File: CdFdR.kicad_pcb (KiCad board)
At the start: 2 copper layers, 64.8 x 90.2 mm, 17 parts, among them J1 Moteur_1, J2 Moteur_2, J3 Moteur_3, J4 Moteur_4, U1 ESP32-S3-N16R8-DEVBOARD

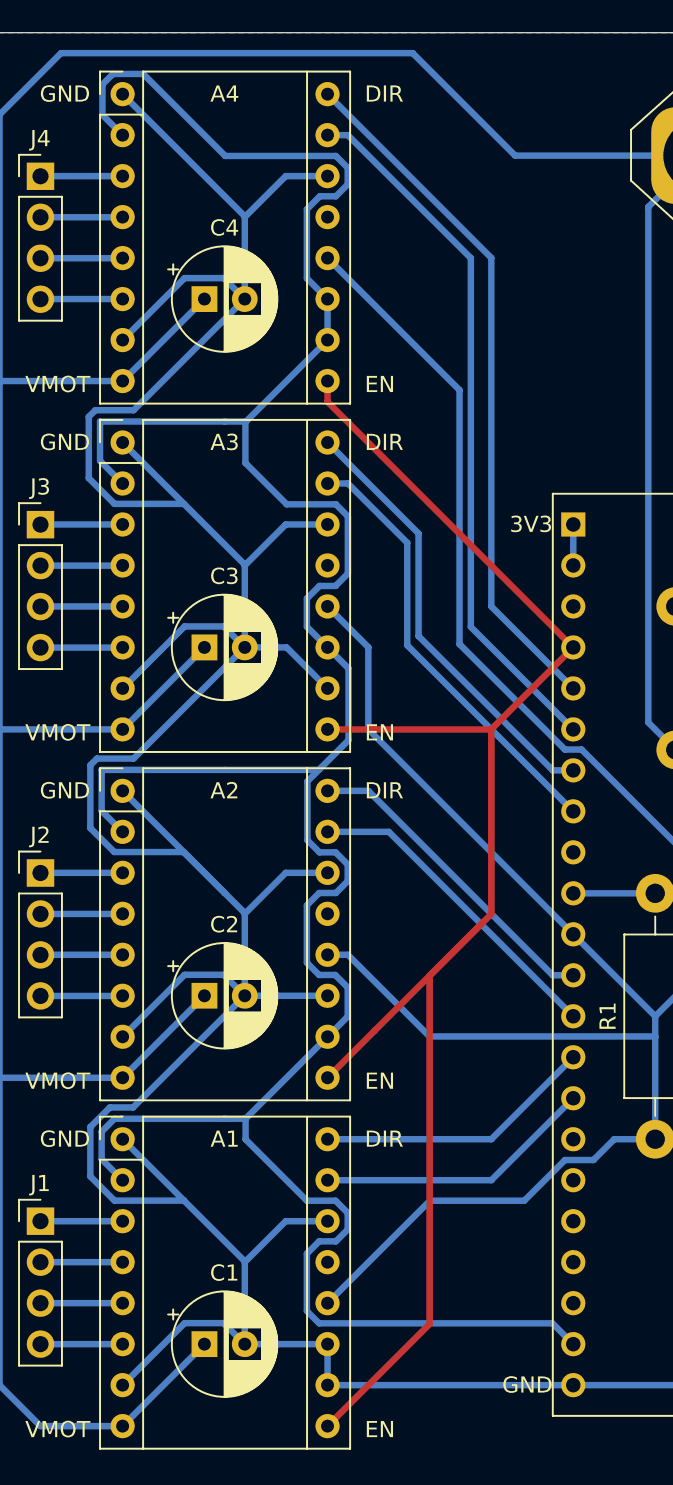
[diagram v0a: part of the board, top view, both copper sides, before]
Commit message: Changed drivers uart code due to error on hand soldered board
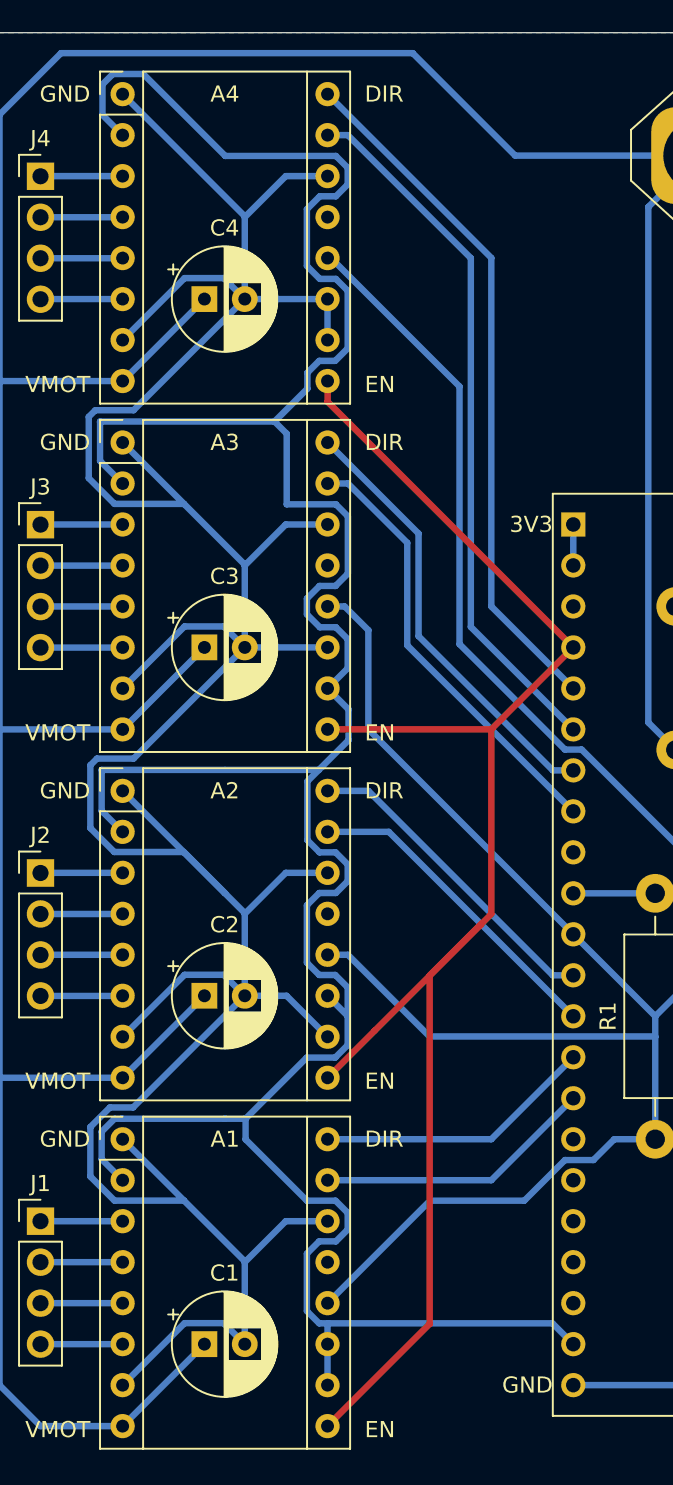
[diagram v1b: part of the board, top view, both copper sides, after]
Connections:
- A1 pad 10: GND -> +5V
- A1 pad 11: GND -> +5V
- A2 pad 10: +5V -> GND
- A2 pad 11: GND -> +5V
- A3 pad 10: GND -> +5V
- A3 pad 11: +5V -> GND
- A4 pad 10: +5V -> GND
- A4 pad 11: +5V -> GND
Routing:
- net GND: track 358.9 -> 343.6 mm
- net +5V: track 179.2 -> 190.0 mm
- net UART_Mot: track 145.8 -> 146.5 mm

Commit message: Correction des pins des moteurs pour être en accord avec carte soudé
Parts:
- A1: value Pololu_Breakout -> M4
- A2: value Pololu_Breakout -> M3
- A3: value Pololu_Breakout -> M2
- A4: value Pololu_Breakout -> M1
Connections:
- A1 pad 15: M1_STP -> M4_STP
- A1 pad 16: M1_DIR -> M4_DIR
- A2 pad 15: M2_STP -> M3_STP
- A2 pad 16: M2_DIR -> M3_DIR
- A3 pad 15: M3_STP -> M2_STP
- A3 pad 16: M3_DIR -> M2_DIR
- A4 pad 15: M4_STP -> M1_STP
- A4 pad 16: M4_DIR -> M1_DIR
- U1 pad 12: M2_DIR -> M3_DIR
- U1 pad 13: M2_STP -> M3_STP
- U1 pad 14: M1_DIR -> M4_DIR
- U1 pad 15: M1_STP -> M4_STP
- U1 pad 5: M4_DIR -> M1_DIR
- U1 pad 6: M4_STP -> M1_STP
- U1 pad 7: M3_DIR -> M2_DIR
- U1 pad 8: M3_STP -> M2_STP
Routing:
- net M4_STP: track 43.9 -> 17.3 mm
- net M1_STP: track 17.3 -> 43.9 mm
- net M4_DIR: track 43.1 -> 17.3 mm
- net M1_DIR: track 17.3 -> 43.1 mm
- net M3_DIR: track 27.4 -> 20.0 mm
- net M2_DIR: track 20.0 -> 27.4 mm
- net M3_STP: track 27.4 -> 20.0 mm
- net M2_STP: track 20.0 -> 27.4 mm
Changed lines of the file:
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@@
 			)
 		)
-		(property "Value" "Pololu_Breakout"
+		(property "Value" "M4"
 			(at 6.35 20.17 0)
 			(layer "F.Fab")
@@
 			(layers "*.Cu" "*.Mask")
 			(remove_unused_layers no)
-			(net 9 "M1_STP")
+			(net 28 "M4_STP")
 			(pinfunction "STEP")
 			(pintype "input")
@@
 			(layers "*.Cu" "*.Mask")
 			(remove_unused_layers no)
-			(net 11 "M1_DIR")
+			(net 33 "M4_DIR")
 			(pinfunction "DIR")
 			(pintype "input")
@@
 			)
 		)
-		(property "Value" "Pololu_Breakout"
+		(property "Value" "M2"
 			(at 6.35 20.17 0)
 			(layer "F.Fab")
@@
 			(layers "*.Cu" "*.Mask")
 			(remove_unused_layers no)
-			(net 22 "M3_STP")
+			(net 18 "M2_STP")
 			(pinfunction "STEP")
 			(pintype "input")
@@
 			(layers "*.Cu" "*.Mask")
 			(remove_unused_layers no)
-			(net 24 "M3_DIR")
+			(net 13 "M2_DIR")
 			(pinfunction "DIR")
 			(pintype "input")
@@
 			)
 		)
-		(property "Value" "Pololu_Breakout"
+		(property "Value" "M3"
 			(at 6.35 20.17 0)
 			(layer "F.Fab")
@@
 			(layers "*.Cu" "*.Mask")
 			(remove_unused_layers no)
-			(net 18 "M2_STP")
+			(net 22 "M3_STP")
 			(pinfunction "STEP")
 			(pintype "input")
@@
 			(layers "*.Cu" "*.Mask")
 			(remove_unused_layers no)
-			(net 13 "M2_DIR")
+			(net 24 "M3_DIR")
 			(pinfunction "DIR")
 			(pintype "input")
@@
 			)
 		)
-		(property "Value" "Pololu_Breakout"
+		(property "Value" "M1"
 			(at 6.35 20.17 0)
 			(layer "F.Fab")
@@
 			(layers "*.Cu" "*.Mask")
 			(remove_unused_layers no)
-			(net 28 "M4_STP")
+			(net 9 "M1_STP")
 			(pinfunction "STEP")
 			(pintype "input")
@@
 			(layers "*.Cu" "*.Mask")
 			(remove_unused_layers no)
-			(net 33 "M4_DIR")
+			(net 11 "M1_DIR")
 			(pinfunction "DIR")
 			(pintype "input")
@@
 			(keep_end_layers yes)
 			(zone_layer_connections)
-			(net 33 "M4_DIR")
+			(net 11 "M1_DIR")
 			(pinfunction "5")
 			(pintype "bidirectional")
@@
 			(keep_end_layers yes)
 			(zone_layer_connections)
-			(net 28 "M4_STP")
+			(net 9 "M1_STP")
 			(pinfunction "6")
 			(pintype "bidirectional")
@@
 			(keep_end_layers yes)
 			(zone_layer_connections)
-			(net 24 "M3_DIR")
+			(net 13 "M2_DIR")
 			(pinfunction "7")
 			(pintype "bidirectional")
@@
 			(keep_end_layers yes)
 			(zone_layer_connections)
-			(net 22 "M3_STP")
+			(net 18 "M2_STP")
 			(pinfunction "15")
 			(pintype "bidirectional")
@@
 			(keep_end_layers yes)
 			(zone_layer_connections)
-			(net 13 "M2_DIR")
+			(net 24 "M3_DIR")
 			(pinfunction "8")
 			(pintype "bidirectional")
@@
 			(keep_end_layers yes)
 			(zone_layer_connections)
-			(net 18 "M2_STP")
+			(net 22 "M3_STP")
 			(pinfunction "3")
 			(pintype "bidirectional")
@@
 			(keep_end_layers yes)
 			(zone_layer_connections)
-			(net 11 "M1_DIR")
+			(net 33 "M4_DIR")
 			(pinfunction "46")
 			(pintype "bidirectional")
@@
 			(keep_end_layers yes)
 			(zone_layer_connections)
-			(net 9 "M1_STP")
+			(net 28 "M4_STP")
 			(pinfunction "9")
 			(pintype "bidirectional")
@@
 	)
 	(segment
-		(start 74.94 119.38)
-		(end 85.09 119.38)
+		(start 76.2 54.61)
+		(end 83.82 62.23)
 		(width 0.4)
 		(layer "B.Cu")
@@
 	)
 	(segment
-		(start 85.09 119.38)
-		(end 90.17 114.3)
+		(start 74.94 54.61)
+		(end 76.2 54.61)
+		(width 0.4)
+		(layer "B.Cu")
+		(net 9)
+	)
+	(segment
+		(start 83.82 62.23)
+		(end 83.82 85.09)
+		(width 0.4)
+		(layer "B.Cu")
+		(net 9)
+	)
+	(segment
+		(start 83.82 85.09)
+		(end 90.17 91.44)
 		(width 0.4)
 		(layer "B.Cu")
@@
 	)
 	(segment
-		(start 85.09 116.84)
-		(end 74.94 116.84)
+		(start 85.09 83.82)
+		(end 85.09 62.22)
 		(width 0.4)
 		(layer "B.Cu")
@@
 	)
 	(segment
-		(start 90.17 111.76)
-		(end 85.09 116.84)
+		(start 85.09 62.22)
+		(end 74.94 52.07)
 		(width 0.4)
 		(layer "B.Cu")
@@
 	)
 	(segment
-		(start 88.9 106.68)
-		(end 77.47 95.25)
+		(start 90.17 88.9)
+		(end 85.09 83.82)
+		(width 0.4)
+		(layer "B.Cu")
+		(net 11)
+	)
+	(segment
+		(start 74.94 73.66)
+		(end 80.58 79.3)
 		(width 0.4)
 		(layer "B.Cu")
@@
 	)
 	(segment
-		(start 90.17 106.68)
-		(end 88.9 106.68)
+		(start 80.58 79.3)
+		(end 80.58 85.66)
 		(width 0.4)
 		(layer "B.Cu")
@@
 	)
 	(segment
-		(start 77.47 95.25)
-		(end 74.94 95.25)
+		(start 88.9 93.98)
+		(end 90.17 93.98)
+		(width 0.4)
+		(layer "B.Cu")
+		(net 13)
+	)
+	(segment
+		(start 80.58 85.66)
+		(end 88.9 93.98)
 		(width 0.4)
 		(layer "B.Cu")
@@
 	)
 	(segment
-		(start 74.94 97.79)
-		(end 78.74 97.79)
+		(start 79.88 86.23)
+		(end 90.17 96.52)
 		(width 0.4)
 		(layer "B.Cu")
@@
 	)
 	(segment
-		(start 78.74 97.79)
-		(end 90.17 109.22)
+		(start 76.205 76.2)
+		(end 79.88 79.875)
+		(width 0.4)
+		(layer "B.Cu")
+		(net 18)
+	)
+	(segment
+		(start 79.88 79.875)
+		(end 79.88 86.23)
+		(width 0.4)
+		(layer "B.Cu")
+		(net 18)
+	)
+	(segment
+		(start 74.94 76.2)
+		(end 76.205 76.2)
 		(width 0.4)
 		(layer "B.Cu")
@@
 	)
 	(segment
-		(start 79.88 86.23)
-		(end 90.17 96.52)
-		(width 0.4)
-		(layer "B.Cu")
-		(net 22)
-	)
-	(segment
-		(start 76.205 76.2)
-		(end 79.88 79.875)
-		(width 0.4)
-		(layer "B.Cu")
-		(net 22)
-	)
-	(segment
-		(start 79.88 79.875)
-		(end 79.88 86.23)
+		(start 74.94 97.79)
+		(end 78.74 97.79)
 		(width 0.4)
 		(layer "B.Cu")
@@
 	)
 	(segment
-		(start 74.94 76.2)
-		(end 76.205 76.2)
+		(start 78.74 97.79)
+		(end 90.17 109.22)
 		(width 0.4)
 		(layer "B.Cu")
@@
 	)
 	(segment
-		(start 74.94 73.66)
-		(end 80.58 79.3)
-		(width 0.4)
-		(layer "B.Cu")
-		(net 24)
-	)
-	(segment
-		(start 80.58 79.3)
-		(end 80.58 85.66)
+		(start 88.9 106.68)
+		(end 77.47 95.25)
 		(width 0.4)
 		(layer "B.Cu")
@@
 	)
 	(segment
-		(start 88.9 93.98)
-		(end 90.17 93.98)
+		(start 90.17 106.68)
+		(end 88.9 106.68)
 		(width 0.4)
 		(layer "B.Cu")
@@
 	)
 	(segment
-		(start 80.58 85.66)
-		(end 88.9 93.98)
+		(start 77.47 95.25)
+		(end 74.94 95.25)
 		(width 0.4)
 		(layer "B.Cu")
@@
 	)
 	(segment
-		(start 76.2 54.61)
-		(end 83.82 62.23)
-		(width 0.4)
-		(layer "B.Cu")
-		(net 28)
-	)
-	(segment
-		(start 74.94 54.61)
-		(end 76.2 54.61)
-		(width 0.4)
-		(layer "B.Cu")
-		(net 28)
-	)
-	(segment
-		(start 83.82 62.23)
-		(end 83.82 85.09)
+		(start 74.94 119.38)
+		(end 85.09 119.38)
 		(width 0.4)
 		(layer "B.Cu")
@@
 	)
 	(segment
-		(start 83.82 85.09)
-		(end 90.17 91.44)
+		(start 85.09 119.38)
+		(end 90.17 114.3)
 		(width 0.4)
 		(layer "B.Cu")
@@
 	)
 	(segment
-		(start 85.09 83.82)
-		(end 85.09 62.22)
-		(width 0.4)
-		(layer "B.Cu")
-		(net 33)
-	)
-	(segment
-		(start 85.09 62.22)
-		(end 74.94 52.07)
+		(start 85.09 116.84)
+		(end 74.94 116.84)
 		(width 0.4)
 		(layer "B.Cu")
@@
 	)
 	(segment
-		(start 90.17 88.9)
-		(end 85.09 83.82)
+		(start 90.17 111.76)
+		(end 85.09 116.84)
 		(width 0.4)
 		(layer "B.Cu")

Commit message: Version envoyé pour vérif
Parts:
- added C5: 100uF/35V, Capacitor_THT:CP_Radial_D6.3mm_P2.50mm, F.Cu at (66.8, 157.7)
- added C6: 100uF/35V, Capacitor_THT:CP_Radial_D6.3mm_P2.50mm, F.Cu at (66.8, 177.8)
- added C7: 2200 uF, Capacitor_THT:CP_Radial_D16.0mm_P7.50mm, F.Cu at (88.5, 55.5)
- added D1: FR107, Diode_THT:D_DO-41_SOD81_P7.62mm_Horizontal, F.Cu at (122.7, 122.0)
- added D2: FR107, Diode_THT:D_DO-41_SOD81_P7.62mm_Horizontal, F.Cu at (122.6, 147.7)
- added D3: FR107, Diode_THT:D_DO-41_SOD81_P7.62mm_Horizontal, F.Cu at (119.8, 186.1)
- added D4: FR107, Diode_THT:D_DO-41_SOD81_P7.62mm_Horizontal, F.Cu at (106.8, 186.1)
- added Electro1: ElectroAimant, Connector_JST:JST_XH_B2B-XH-A_1x02_P2.50mm_Vertical, F.Cu at (126.3, 182.0)
- added Electro2: ElectroAimant, Connector_JST:JST_XH_B2B-XH-A_1x02_P2.50mm_Vertical, F.Cu at (113.3, 182.0)
- added Fan1: Fan, Connector_JST:JST_XH_B2B-XH-A_1x02_P2.50mm_Vertical, F.Cu at (132.0, 85.0)
- added Fan2: Fan, Connector_JST:JST_XH_B2B-XH-A_1x02_P2.50mm_Vertical, F.Cu at (132.0, 76.5)
- added G***: LOGO, LOGO, F.Cu at (96.5, 171.5)
- added H1: MountingHole, MountingHole:MountingHole_3.2mm_M3, F.Cu at (56.0, 53.0)
- added H2: MountingHole, MountingHole:MountingHole_3.2mm_M3, F.Cu at (135.5, 53.0)
- added H3: MountingHole, MountingHole:MountingHole_3.2mm_M3, F.Cu at (56.0, 184.0)
- added H4: MountingHole, MountingHole:MountingHole_3.2mm_M3, F.Cu at (135.5, 184.0)
- added J5: Nema17_5, Connector_JST:JST_XH_B4B-XH-A_1x04_P2.50mm_Vertical, F.Cu at (56.5, 149.2)
- added J6: Nema17_6, Connector_JST:JST_XH_B4B-XH-A_1x04_P2.50mm_Vertical, F.Cu at (56.5, 169.0)
- added J7: IHM, Connector_JST:JST_XH_B4B-XH-A_1x04_P2.50mm_Vertical, F.Cu at (134.5, 96.5)
- added J8: Lidar, Connector_JST:JST_XH_B4B-XH-A_1x04_P2.50mm_Vertical, F.Cu at (120.5, 96.5)
- added Module_LM2596: LM2596, Custom:LM2596 Converter DC-DC, F.Cu at (104.5, 79.5)
- added PUMP-1: PUMP, Connector_JST:JST_XH_B2B-XH-A_1x02_P2.50mm_Vertical, F.Cu at (133.0, 130.0)
- added PUMP-2: PUMP, Connector_JST:JST_XH_B2B-XH-A_1x02_P2.50mm_Vertical, F.Cu at (132.5, 155.7)
- added Q1: IRLZ44N, Package_TO_SOT_THT:TO-220-3_Vertical, F.Cu at (132.5, 117.0)
- added Q2: IRLZ44N, Package_TO_SOT_THT:TO-220-3_Vertical, F.Cu at (132.0, 142.5)
- added Q3: IRLZ44N, Package_TO_SOT_THT:TO-220-3_Vertical, F.Cu at (129.2, 174.4)
- added Q4: IRLZ44N, Package_TO_SOT_THT:TO-220-3_Vertical, F.Cu at (116.2, 174.5)
- added R10: 330, Resistor_THT:R_Axial_DIN0207_L6.3mm_D2.5mm_P7.62mm_Horizontal, F.Cu at (122.3, 165.5)
- added R11: 10k, Resistor_THT:R_Axial_DIN0207_L6.3mm_D2.5mm_P7.62mm_Horizontal, F.Cu at (122.3, 169.0)
- added R12: 1k, Resistor_THT:R_Axial_DIN0207_L6.3mm_D2.5mm_P7.62mm_Horizontal, F.Cu at (107.5, 120.4)
- added R4: 330, Resistor_THT:R_Axial_DIN0207_L6.3mm_D2.5mm_P7.62mm_Horizontal, F.Cu at (123.0, 110.9)
- added R5: 10k, Resistor_THT:R_Axial_DIN0207_L6.3mm_D2.5mm_P7.62mm_Horizontal, F.Cu at (127.0, 110.7)
- added R6: 330, Resistor_THT:R_Axial_DIN0207_L6.3mm_D2.5mm_P7.62mm_Horizontal, F.Cu at (123.0, 136.4)
- added R7: 10k, Resistor_THT:R_Axial_DIN0207_L6.3mm_D2.5mm_P7.62mm_Horizontal, F.Cu at (126.5, 136.4)
- added R8: 330, Resistor_THT:R_Axial_DIN0207_L6.3mm_D2.5mm_P7.62mm_Horizontal, F.Cu at (130.0, 162.0)
- added R9: 10k, Resistor_THT:R_Axial_DIN0207_L6.3mm_D2.5mm_P7.62mm_Horizontal, F.Cu at (133.5, 162.0)
- added SW1: Alim_generale, Connector_AMASS:AMASS_XT60-F_1x02_P7.20mm_Vertical, F.Cu at (114.0, 62.5)
- added SW2: Tirette, Connector_JST:JST_XH_B2B-XH-A_1x02_P2.50mm_Vertical, F.Cu at (85.5, 178.0)
- added SW3: Urgence, Connector_AMASS:AMASS_XT60-F_1x02_P7.20mm_Vertical, F.Cu at (103.0, 62.5)
- added TMC-MC1: Pololu_Breakout, Custom:Pololu_Breakout-16_15.2x20.3mm_Better_Silkscreen, F.Cu at (62.0, 144.1)
- added TMC-MC2: Pololu_Breakout, Custom:Pololu_Breakout-16_15.2x20.3mm_Better_Silkscreen, F.Cu at (62.0, 166.5)
- added VALVE-1: VALVE, Connector_JST:JST_XH_B2B-XH-A_1x02_P2.50mm_Vertical, F.Cu at (123.5, 130.0)
- added VALVE-2: VALVE, Connector_JST:JST_XH_B2B-XH-A_1x02_P2.50mm_Vertical, F.Cu at (124.0, 155.7)
- J1: value Moteur_1 -> Nema17_1; footprint Connector_PinHeader_2.54mm:PinHeader_1x04_P2.54mm_Vertical -> Connector_JST:JST_XH_B4B-XH-A_1x04_P2.50mm_Vertical
- J2: value Moteur_2 -> Nema17_2; footprint Connector_PinHeader_2.54mm:PinHeader_1x04_P2.54mm_Vertical -> Connector_JST:JST_XH_B4B-XH-A_1x04_P2.50mm_Vertical
- J3: value Moteur_3 -> Nema17_3; footprint Connector_PinHeader_2.54mm:PinHeader_1x04_P2.54mm_Vertical -> Connector_JST:JST_XH_B4B-XH-A_1x04_P2.50mm_Vertical
- J4: value Moteur_4 -> Nema17_4; footprint Connector_PinHeader_2.54mm:PinHeader_1x04_P2.54mm_Vertical -> Connector_JST:JST_XH_B4B-XH-A_1x04_P2.50mm_Vertical
- R1, R2, R3: footprint Resistor_THT:R_Axial_DIN0411_L9.9mm_D3.6mm_P15.24mm_Horizontal -> Resistor_THT:R_Axial_DIN0207_L6.3mm_D2.5mm_P7.62mm_Horizontal
- TMC-ROUE1: renamed from A1; value M4 -> Pololu_Breakout
- TMC-ROUE2: renamed from A2; value M3 -> Pololu_Breakout
- TMC-ROUE3: renamed from A3; value M2 -> Pololu_Breakout
- TMC-ROUE4: renamed from A4; value M1 -> Pololu_Breakout
- moved C4 70.5 mm to (66.8, 135.2)
- moved TMC-ROUE4 69.5 mm to (62.0, 121.5)
- moved J4 69.4 mm to (56.5, 126.5), turned to -90 degrees
- moved TMC-ROUE1 62.5 mm to (62.0, 54.4)
- moved C1 61.5 mm to (66.8, 68.1)
- moved J1 60.4 mm to (56.5, 61.5), turned to -90 degrees
- moved R2 43.5 mm to (101.0, 127.1), turned to 90 degrees
- moved U1 29.0 mm to (87.6, 107.6)
- moved BT1 27.8 mm to (125.0, 62.5), turned to 90 degrees
- moved C3 27.0 mm to (66.8, 113.4)
- moved J3 25.6 mm to (56.5, 104.4), turned to -90 degrees
- moved TMC-ROUE3 25.5 mm to (62.0, 99.2)
- moved TMC-ROUE2 18.7 mm to (62.0, 76.6)
- moved J2 18.6 mm to (56.5, 81.7), turned to -90 degrees
- moved C2 17.7 mm to (66.8, 90.3)
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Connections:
- BT1 pad 1: +BATT -> Net-(BT1-+)
- C1 pad 1: +BATT -> +24V
- C2 pad 1: +BATT -> +24V
- C3 pad 1: +BATT -> +24V
- C4 pad 1: +BATT -> +24V
- R1 pad 1: UART_Mot -> Net-(U1-17)
- R1 pad 2: /TX1 -> UART_Mot
- R3 pad 1: +BATT -> V_Batt
- TMC-ROUE1 pad 10: +5V -> GND
- TMC-ROUE1 pad 11: +5V -> GND
- TMC-ROUE1 pad 15: M4_STP -> M1_STP
- TMC-ROUE1 pad 16: M4_DIR -> M1_DIR
- TMC-ROUE1 pad 2: +5V -> +3.3V
- TMC-ROUE1 pad 8: +BATT -> +24V
- TMC-ROUE2 pad 10: GND -> +3.3V
- TMC-ROUE2 pad 11: +5V -> GND
- TMC-ROUE2 pad 15: M3_STP -> M2_STP
- TMC-ROUE2 pad 16: M3_DIR -> M2_DIR
- TMC-ROUE2 pad 2: +5V -> +3.3V
- TMC-ROUE2 pad 8: +BATT -> +24V
- TMC-ROUE3 pad 10: +5V -> GND
- TMC-ROUE3 pad 11: GND -> +3.3V
- TMC-ROUE3 pad 15: M2_STP -> M3_STP
- TMC-ROUE3 pad 16: M2_DIR -> M3_DIR
- TMC-ROUE3 pad 2: +5V -> +3.3V
- TMC-ROUE3 pad 8: +BATT -> +24V
- TMC-ROUE4 pad 10: GND -> +3.3V
- TMC-ROUE4 pad 11: GND -> +3.3V
- TMC-ROUE4 pad 15: M1_STP -> M4_STP
- TMC-ROUE4 pad 16: M1_DIR -> M4_DIR
- TMC-ROUE4 pad 2: +5V -> +3.3V
- TMC-ROUE4 pad 8: +BATT -> +24V
- U1 pad 1: Net-(U1-3V3-Pad1) -> +3.3V
- U1 pad 10: /TX1 -> Net-(U1-17)
- U1 pad 14: M4_DIR -> unconnected-(U1-46-Pad14)
- U1 pad 15: M4_STP -> M4_DIR
- U1 pad 16: unconnected-(U1-10-Pad16) -> M4_STP
- U1 pad 17: unconnected-(U1-11-Pad17) -> M5_DIR
- U1 pad 18: unconnected-(U1-12-Pad18) -> M5_STP
- U1 pad 19: unconnected-(U1-13-Pad19) -> M6_DIR
- U1 pad 2: Net-(U1-3V3-Pad1) -> +3.3V
- U1 pad 20: unconnected-(U1-14-Pad20) -> M6_STP
- U1 pad 27: unconnected-(U1-21-Pad27) -> Net-(U1-21)
- U1 pad 28: unconnected-(U1-47-Pad28) -> ELECTRO2
- U1 pad 29: unconnected-(U1-48-Pad29) -> ELECTRO1
- U1 pad 35: unconnected-(U1-38-Pad35) -> PUMP_VALVE2
- U1 pad 36: unconnected-(U1-39-Pad36) -> PUMP_VALVE1
- U1 pad 37: unconnected-(U1-40-Pad37) -> CLK_IHM
- U1 pad 38: unconnected-(U1-41-Pad38) -> DIO_IHM
- U1 pad 39: unconnected-(U1-42-Pad39) -> Net-(U1-42)
- U1 pad 4: Drive_Mot_EN -> M1_DIR
- U1 pad 40: unconnected-(U1-2-Pad40) -> UART_Chariot
- U1 pad 42: unconnected-(U1-44-Pad42) -> TX_Lidar
- U1 pad 5: M1_DIR -> M1_STP
- U1 pad 6: M1_STP -> M2_DIR
- U1 pad 7: M2_DIR -> M2_STP
- U1 pad 8: M2_STP -> Drive_Mot_EN
- U1 pad 9: unconnected-(U1-16-Pad9) -> Drive_Chariot_EN
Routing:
- net +24V: track 0.00 -> 412.2 mm
- net +3.3V: track 0.00 -> 278.3 mm
- net GND: track 343.6 -> 601.6 mm, vias 0 -> 2
- net +BATT: track 225.5 -> 0.00 mm
- net Drive_Chariot_EN: track 0.00 -> 95.5 mm, vias 0 -> 2
- net UART_Chariot: track 0.00 -> 93.0 mm, vias 0 -> 1
- net V_Batt: track 0.00 -> 87.2 mm
- net +5V: track 190.0 -> 117.5 mm
- net Net-(U1-21): track 0.00 -> 38.5 mm
- net CLK_IHM: track 0.00 -> 37.8 mm
- net DIO_IHM: track 0.00 -> 34.2 mm
- net ELECTRO1: track 0.00 -> 28.9 mm
- net Net-(D1-A): track 0.00 -> 27.8 mm
- net UART_Mot: track 146.5 -> 119.8 mm, vias 0 -> 2
- net M2_STP: track 27.4 -> 53.5 mm
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- added copper zone on F.Cu, net GND
- removed copper zone on B.Cu, net GND
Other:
- board size 64.8 x 90.2 mm -> 91.5 x 143 mm
- board text added: "100k"
- board text added: "10k"
- board text added: "15k"
- board text added: "1k"
- board text added: "2025"
- board text added: "2200uF"
- board text added: "330"
- board text added: "BAU"
- board text added: "Batterie"
- board text added: "Btn_General"
- board text added: "Coupe de France de Robotique"
- board text added: "DIR"
